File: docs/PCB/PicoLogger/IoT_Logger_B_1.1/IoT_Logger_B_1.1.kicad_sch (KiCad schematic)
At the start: 31 parts, among them J1 JTAG, U1 STM32F412RGTx, Y1 3225-25M-SR, Y2 32.768K-CFPX217

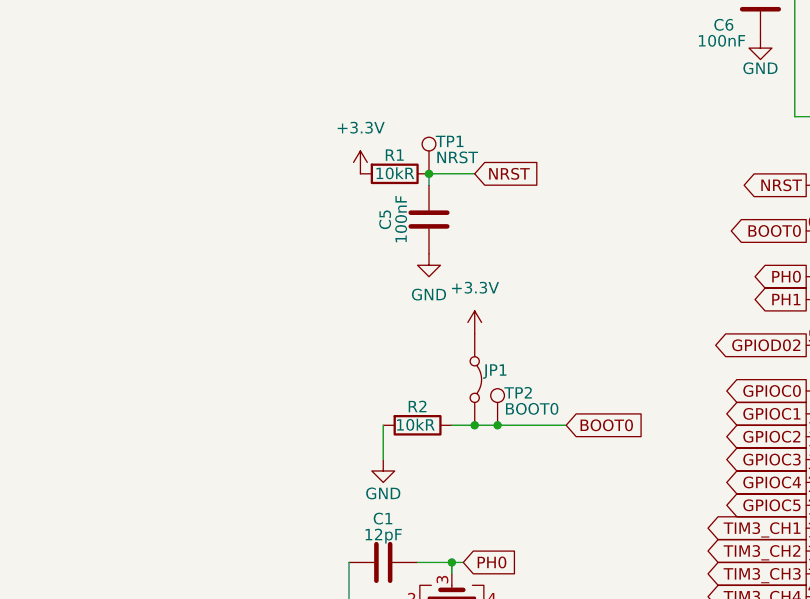
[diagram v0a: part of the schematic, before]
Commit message: New logger revisions added.
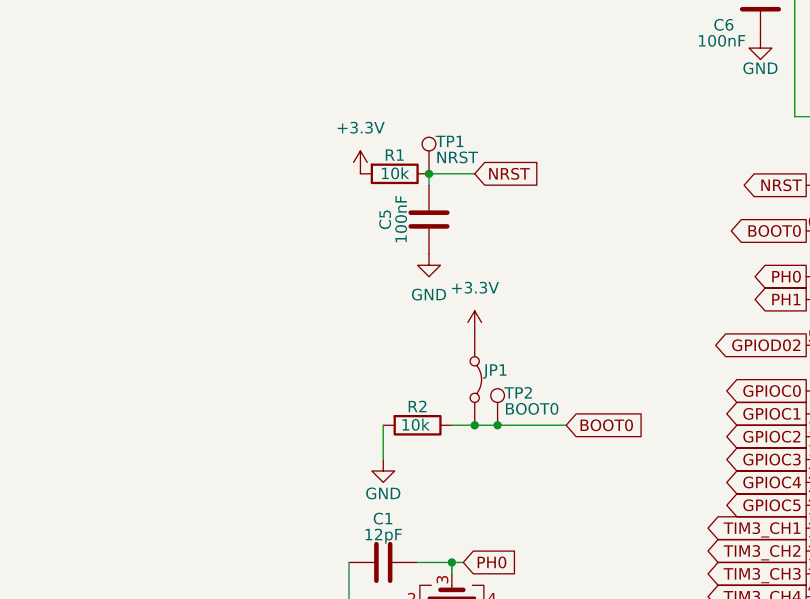
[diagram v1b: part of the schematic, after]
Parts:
- R1, R2: value 10kR -> 10k
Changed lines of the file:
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@@
 			)
 		)
-		(property "Value" "10kR"
+		(property "Value" "10k"
 			(at 87.376 101.6 90)
 			(effects
@@
 			)
 		)
-		(property "Value" "10kR"
+		(property "Value" "10k"
 			(at 85.09 73.66 90)
 			(effects
